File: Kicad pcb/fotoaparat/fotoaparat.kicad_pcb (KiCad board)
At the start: 2 copper layers, 120 x 85 mm, 75 parts, among them IC1 Lineární Regulátor, IC3 Lineární Regulátor Displaye, U1 STM32L496RETx, U2 MCP73833-FCI/UN, Y1 8mhz krystal

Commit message: Pokus o druhý prototyp
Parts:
- removed +BATT: Baterie, Connector_PinSocket_2.54mm:PinSocket_1x02_P2.54mm_Horizontal
- removed CAMERA: Kamera, Connector_PinSocket_2.54mm:PinSocket_2x11_P2.54mm_Vertical
- removed Free Pins: Conn_01x11_Socket, Connector_PinSocket_2.54mm:PinSocket_1x11_P2.54mm_Horizontal
- removed LCD: LCD konektor, FFC2A32-20-T:GCT_FFC2A32-20-T
- removed RX: UART, Connector_PinHeader_2.54mm:PinHeader_1x02_P2.54mm_Vertical
- removed SD CARD: GSD090012SEU, gsd09:GSD090012SEU_AMP
- removed SWD: SWD, Connector_PinHeader_2.54mm:PinHeader_1x04_P2.54mm_Vertical
- removed USB: USB Konektor, 47436:473460001
- added J1: USB Konektor, 47436:473460001, F.Cu at (207.0, 97.0)
- added J2: SWD, Connector_PinHeader_2.54mm:PinHeader_1x04_P2.54mm_Vertical, F.Cu at (155.7, 88.2)
- added J3: LCD konektor, FFC2A32-20-T:GCT_FFC2A32-20-T, F.Cu at (102.6, 97.9)
- added J4: Baterie, Connector_PinSocket_2.54mm:PinSocket_1x02_P2.54mm_Horizontal, F.Cu at (92.1, 73.8)
- added J5: GSD090012SEU, gsd09:GSD090012SEU_AMP, F.Cu at (195.0, 121.0)
- added J6: UART, Connector_PinHeader_2.54mm:PinHeader_1x02_P2.54mm_Vertical, F.Cu at (126.2, 118.5)
- added J7: Kamera, Connector_PinSocket_2.54mm:PinSocket_2x11_P2.54mm_Vertical, B.Cu at (172.2, 84.9)
- added J9: Conn_01x11_Socket, Connector_PinSocket_2.54mm:PinSocket_1x11_P2.54mm_Horizontal, F.Cu at (175.8, 71.5)
- moved H3 110.7 mm to (197.0, 63.6)
- moved H1 110.3 mm to (86.1, 140.0)
- moved R25 106.1 mm to (95.4, 73.0)
- moved R26 105.8 mm to (95.4, 77.6)
- moved S1 103.5 mm to (84.1, 94.0), turned to 90 degrees
- moved U2 100.5 mm to (94.8, 138.6), turned to 0 degrees
- moved R8 95.6 mm to (187.5, 51.1), turned to 0 degrees
- moved D1 95.3 mm to (102.4, 130.4), turned to 0 degrees
- moved D2 94.8 mm to (102.4, 133.5), turned to 0 degrees
- moved TH1 94.7 mm to (99.2, 76.4), turned to 180 degrees
- moved D3 94.5 mm to (102.4, 136.5), turned to 0 degrees
- moved R13 94.3 mm to (187.5, 65.8), turned to 0 degrees
- moved C2 90.7 mm to (114.8, 54.4), turned to 0 degrees
- moved C1 89.6 mm to (114.8, 51.4), turned to 0 degrees
- moved C5 89.0 mm to (114.8, 63.4), turned to 0 degrees
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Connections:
- net /Backlight Regulátor renamed /Backlight Regulátor en
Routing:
- net +3.3V: track 355.6 -> 17.0 mm, vias 25 -> 0
- net +3.3V LCD: track 170.2 -> 0.00 mm, vias 6 -> 0
- net GND: track 187.3 -> 18.9 mm, vias 37 -> 1
- net /d3: track 106.8 -> 25.3 mm, vias 6 -> 0
- net /d1: track 101.5 -> 24.6 mm, vias 6 -> 0
- net /d0: track 101.4 -> 27.4 mm, vias 9 -> 0
- net +BATT: track 77.7 -> 5.10 mm, vias 2 -> 0
- net /d2: track 99.5 -> 28.0 mm, vias 11 -> 0
- net /pb0: track 64.8 -> 0.00 mm, vias 5 -> 0
- net /rrst: track 49.2 -> 111.8 mm, vias 4 -> 2
- net /pb1: track 61.6 -> 0.00 mm, vias 4 -> 0
- net /pa2: track 49.7 -> 0.00 mm, vias 2 -> 0
- net /rck: track 77.0 -> 126.1 mm, vias 8 -> 0
- net Net-(IC1-EN): track 43.7 -> 0.00 mm
- net Net-(IC3-EN): track 37.0 -> 0.00 mm
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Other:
- board size 120 x 85 mm -> 129 x 86.1 mm

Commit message: Téměř dokončený 2 prototyp
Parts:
- moved R8 92.4 mm to (102.7, 87.9)
- moved R7 90.8 mm to (92.0, 66.7), turned to 90 degrees
- moved R13 86.5 mm to (108.2, 100.3)
- moved R4 79.9 mm to (103.1, 66.7), turned to 180 degrees
- moved R5 74.8 mm to (108.2, 68.4), turned to 180 degrees
- moved U2 72.0 mm to (94.9, 66.6), turned to -90 degrees
- moved D3 71.7 mm to (112.1, 65.5), turned to 90 degrees
- moved R6 70.7 mm to (112.1, 69.2), turned to -90 degrees
- moved D2 68.3 mm to (109.1, 65.5), turned to 90 degrees
- moved C6 65.9 mm to (109.7, 132.1)
- moved D1 65.0 mm to (106.1, 65.5), turned to 90 degrees
- moved C5 64.4 mm to (110.0, 127.6)
- moved C4 63.8 mm to (110.3, 124.0)
- moved C3 63.3 mm to (110.3, 120.5)
- moved R9 37.2 mm to (167.7, 85.5), turned to 180 degrees
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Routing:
- net /pa2: track 0.00 -> 184.6 mm, vias 0 -> 4
- net /pb1: track 0.00 -> 157.9 mm, vias 0 -> 4
- net /pb0: track 0.00 -> 151.9 mm, vias 0 -> 4
- net +BATT: track 5.10 -> 113.5 mm
- net Net-(IC3-EN): track 0.00 -> 67.4 mm, vias 0 -> 4
- net Net-(IC1-EN): track 0.00 -> 50.1 mm, vias 0 -> 4
- net +3.3V LCD: track 0.00 -> 41.3 mm, vias 0 -> 6
- net Net-(U2-*PG): track 0.00 -> 21.2 mm
- net Net-(U2-STAT2): track 0.00 -> 15.5 mm
- net Net-(U2-THERM): track 0.00 -> 13.5 mm
- net /Vled+: track 0.00 -> 10.5 mm
- net Net-(U2-STAT1): track 0.00 -> 8.80 mm
- net /pb12: track 51.9 -> 46.3 mm, vias 1 -> 2
- net /pd2: track 38.6 -> 42.4 mm, vias 1 -> 2
- net /im3: track 0.00 -> 3.47 mm
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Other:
- board size 129 x 86.1 mm -> 128.9 x 86.1 mm

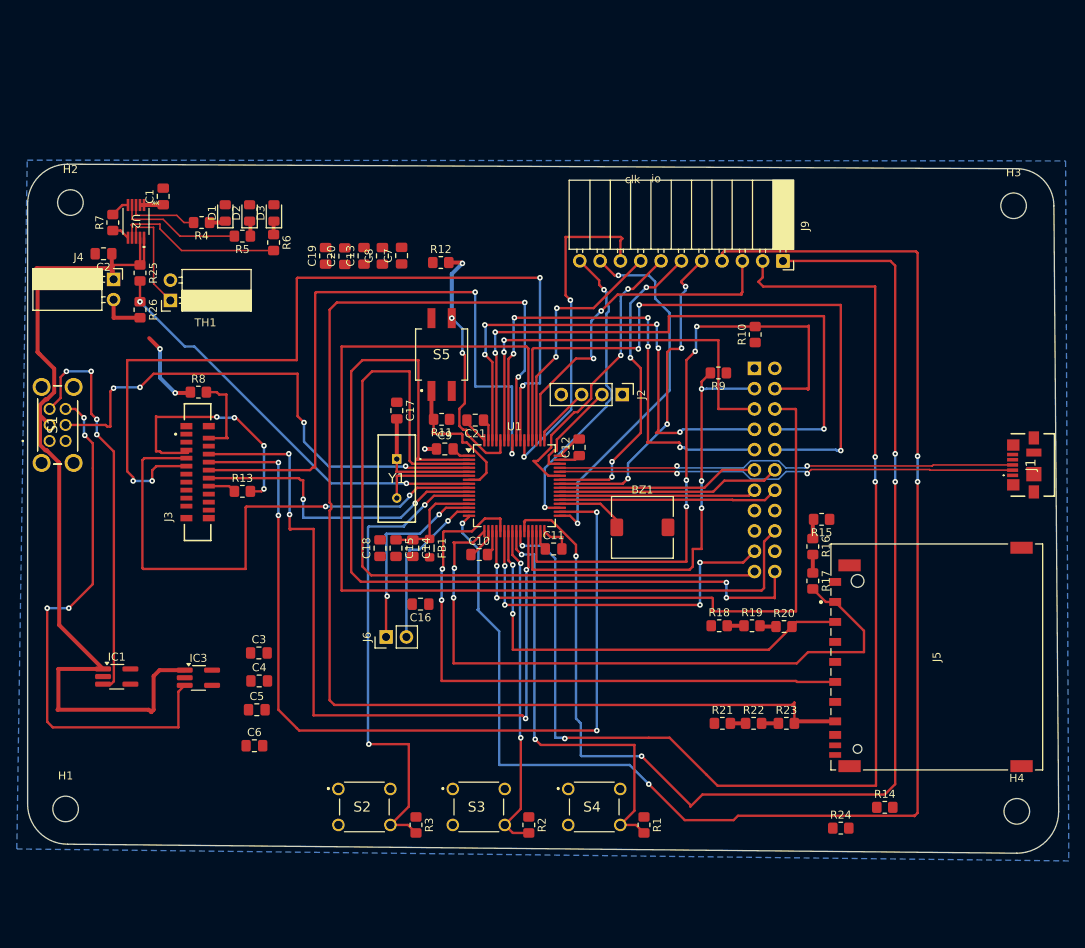
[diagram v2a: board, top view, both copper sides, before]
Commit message: Druhá deska pcb
Signálové trasy jsou víc daleko od sebe a napájecí trasy jsou více široké než v minulém designu, to by mělo zmírnit elektromagnetickou interferenci.
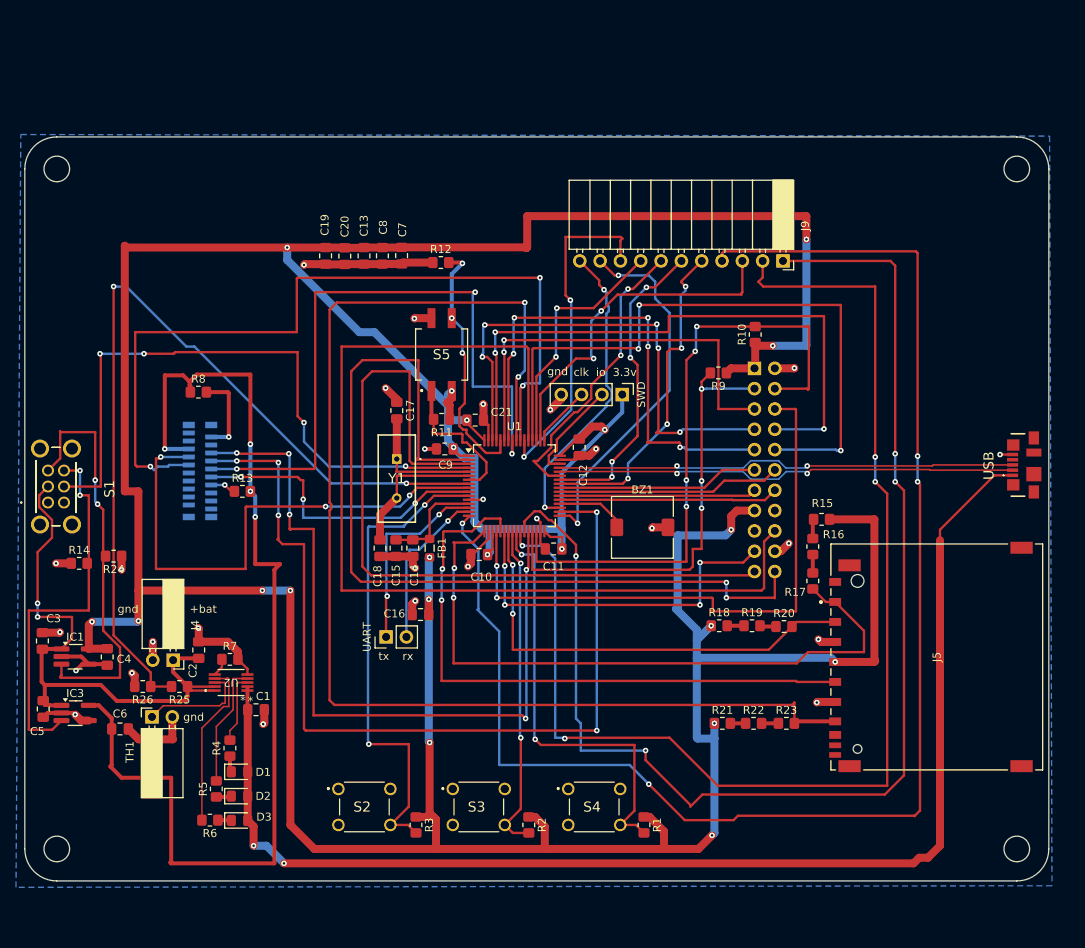
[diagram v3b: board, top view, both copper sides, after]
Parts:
- LCD: renamed from J3; moved to B.Cu
- moved R14 105.2 mm to (87.8, 109.3)
- moved R24 97.1 mm to (92.1, 108.4), turned to 180 degrees
- moved D3 76.1 mm to (107.8, 141.4), turned to 0 degrees
- moved D2 72.9 mm to (107.8, 138.4), turned to 0 degrees
- moved R6 72.6 mm to (104.1, 141.4), turned to 180 degrees
- moved D1 69.9 mm to (107.8, 135.4), turned to 0 degrees
- moved R5 69.2 mm to (104.9, 137.5), turned to 90 degrees
- moved R4 65.8 mm to (106.6, 132.4), turned to 90 degrees
- moved C1 65.2 mm to (109.9, 127.6), turned to 0 degrees
- moved U2 58.9 mm to (106.8, 124.2), turned to 180 degrees
- moved R7 56.5 mm to (106.6, 121.3), turned to 0 degrees
- moved TH1 52.1 mm to (96.9, 128.5), turned to 90 degrees
- moved R25 51.9 mm to (100.3, 124.7), turned to 180 degrees
- moved C2 50.9 mm to (102.7, 120.1), turned to 90 degrees
- moved J4 48.2 mm to (99.5, 121.4), turned to -90 degrees
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- renumbered J7 to CAMERA, J2 to SWD, J6 to UART, J1 to USB
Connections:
- IC1 pad 4: unconnected-(IC1-NC/ADJ-Pad4) -> GND
- IC3 pad 4: unconnected-(IC3-NC/ADJ-Pad4) -> GND
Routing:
- net +3.3V: track 17.0 -> 550.7 mm, vias 0 -> 21
- net VBUS: track 2.80 -> 159.1 mm, vias 0 -> 2
- net GND: track 21.3 -> 113.7 mm, vias 1 -> 28
- net +3.3V LCD: track 41.3 -> 131.3 mm, vias 6 -> 4
- net /Baterka Napětí: track 53.1 -> 109.2 mm
- net +BATT: track 113.5 -> 73.4 mm, vias 0 -> 2
- net Net-(IC3-EN): track 67.4 -> 47.6 mm, vias 4 -> 2
- net /Backlight Regulátor en: track 65.2 -> 79.6 mm
- net /osc out: track 11.8 -> 17.9 mm
- net /csx: track 107.9 -> 103.6 mm, vias 4 -> 3
- net /sda: track 68.8 -> 65.9 mm, vias 2 -> 3
- net /pb1: track 157.9 -> 160.1 mm
- net /pb0: track 151.9 -> 153.9 mm
- net Net-(IC1-EN): track 50.1 -> 51.2 mm, vias 4 -> 2
- net /scl: track 112.4 -> 113.4 mm, vias 4 -> 5
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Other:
- board size 128.9 x 86.1 mm -> 128 x 93 mm
- board text added: "+bat"
- board text added: "3.3v"
- board text added: "gnd"
- board text added: "rx"
- board text added: "tx"

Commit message: Příprava na výrobu pcb
Gerber soubory se pravděpodobně ještě změní
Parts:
- removed CAMERA: Kamera, Connector_PinSocket_2.54mm:PinSocket_2x11_P2.54mm_Vertical
- removed LCD: LCD konektor, FFC2A32-20-T:GCT_FFC2A32-20-T
- added J3: LCD konektor, FFC2A32-20-T:GCT_FFC2A32-20-T, F.Cu at (102.8, 97.7)
- added J7: Kamera, Connector_PinSocket_2.54mm:PinSocket_2x11_P2.54mm_Vertical, F.Cu at (174.7, 84.9)
- SD CARD: renamed from J5
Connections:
- U1 pad 2: /rrst -> /wrst
- U1 pad 20: /href -> /vsync
- U1 pad 3: /wrst -> /rrst
- U1 pad 37: /d0 -> /d1
- U1 pad 38: /d1 -> /d0
- U1 pad 39: /d2 -> /d3
- U1 pad 40: /d3 -> /d2
- U1 pad 52: /d4 -> /d5
- U1 pad 58: /d5 -> /d4
- U1 pad 59: /vsync -> /href
- U1 pad 61: /d6 -> /d7
- U1 pad 62: /d7 -> /d6
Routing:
- net /vsync: track 52.5 -> 77.5 mm
- net /href: track 75.6 -> 52.7 mm
- net /d5: track 62.0 -> 83.7 mm, vias 5 -> 3
- net /d4: track 82.0 -> 63.6 mm, vias 3 -> 5
- net /wr: track 46.3 -> 63.6 mm
- net GND: track 113.7 -> 129.9 mm, vias 28 -> 27
- net /d7: track 63.3 -> 77.3 mm, vias 5 -> 3
- net /rrst: track 111.8 -> 98.0 mm, vias 2 -> 0
- net /wrst: track 98.0 -> 111.7 mm, vias 0 -> 2
- net /d6: track 77.0 -> 64.0 mm, vias 3 -> 5
- net +3.3V: track 550.7 -> 538.7 mm
- net /pa2: track 184.9 -> 190.7 mm
- net /d1: track 24.6 -> 28.9 mm
- net /d3: track 25.3 -> 28.7 mm
- net /I2C_SCL: track 57.4 -> 60.8 mm
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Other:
- board text added: "Battery"

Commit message: Oprava chyb
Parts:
- removed C13, C19, C20, C8: 1u, Capacitor_SMD:C_0805_2012Metric_Pad1.18x1.45mm_HandSolder
- added C22: 1u, Capacitor_SMD:C_0805_2012Metric_Pad1.18x1.45mm_HandSolder, F.Cu at (179.1, 124.1)
- C7: value 1u -> 10u; footprint Capacitor_SMD:C_0805_2012Metric_Pad1.18x1.45mm_HandSolder -> Capacitor_THT:CP_Radial_D5.0mm_P2.50mm
- moved R8 19.6 mm to (102.8, 107.5), turned to 180 degrees
- moved R13 11.2 mm to (98.2, 95.3), turned to 180 degrees
- moved C7 6.29 mm to (128.1, 64.5), turned to -90 degrees
- turned J3 to -90 degrees
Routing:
- net /sda: track 65.9 -> 34.6 mm
- net /csx: track 103.8 -> 87.4 mm
- net GND: track 129.9 -> 118.3 mm
- net /sdo: track 38.6 -> 45.9 mm
- net +3.3V: track 538.7 -> 545.8 mm
- net /wrx d/cx: track 82.0 -> 88.4 mm, vias 2 -> 4
- net +3.3V LCD: track 131.3 -> 125.4 mm, vias 3 -> 0
- net /rst: track 97.2 -> 100.6 mm
- net /scl: track 113.5 -> 115.3 mm
- net /im3: track 3.77 -> 2.43 mm
- net /Vled+: track 10.7 -> 9.43 mm
- net Net-(IC3-EN): track 47.6 -> 46.6 mm
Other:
- board text added: "Dat0 - 7"
- board text added: "href"
- board text added: "nc"
- board text added: "rck"
- board text added: "rrst"
- board text added: "scl"
- board text added: "sda"
- board text added: "vsync"
- board text added: "wr"
- board text added: "wrst"

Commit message: Připraveno na výrobu
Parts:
- added C8: 10u, Capacitor_THT:CP_Radial_D5.0mm_P2.50mm, F.Cu at (181.5, 66.1)
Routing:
- net +3.3V: track 545.8 -> 548.7 mm
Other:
- board text added: "boot0"
- board text added: "reset"

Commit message: Úprava designu
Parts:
- removed C10, C11, C12, C14, C21, C9: 100n, Capacitor_SMD:C_0805_2012Metric_Pad1.18x1.45mm_HandSolder
- removed C15, C16, C22: 1u, Capacitor_SMD:C_0805_2012Metric_Pad1.18x1.45mm_HandSolder
- removed C17, C18: 30p, Capacitor_SMD:C_0805_2012Metric_Pad1.18x1.45mm_HandSolder
- removed C7, C8: 10u, Capacitor_THT:CP_Radial_D5.0mm_P2.50mm
- removed D1, D2, D3: LED, LED_SMD:LED_0805_2012Metric_Pad1.15x1.40mm_HandSolder
- removed FB1: 120R, Inductor_SMD:L_0805_2012Metric_Pad1.05x1.20mm_HandSolder
- removed H1, H2, H3, H4: MountingHole, MountingHole:MountingHole_3.2mm_M3
- removed IC1: Lineární Regulátor, Package_TO_SOT_SMD:TSOT-23-5_HandSoldering
- removed IC3: Lineární Regulátor Displaye, Package_TO_SOT_SMD:TSOT-23-5_HandSoldering
- removed J3: LCD konektor, FFC2A32-20-T:GCT_FFC2A32-20-T
- removed J4: Baterie, Connector_PinSocket_2.54mm:PinSocket_1x02_P2.54mm_Horizontal
- removed J7: Kamera, Connector_PinSocket_2.54mm:PinSocket_2x11_P2.54mm_Vertical
- removed J9: Conn_01x11_Socket, Connector_PinSocket_2.54mm:PinSocket_1x11_P2.54mm_Horizontal
- removed R10, R11, R12, R13, R14, R15, R16, R17, R18, R19, R20, R21, R22, R23, R24, R26, R9: 4.7k, Resistor_SMD:R_0805_2012Metric_Pad1.20x1.40mm_HandSolder
- removed R25, R7: 1k, Resistor_SMD:R_0805_2012Metric_Pad1.20x1.40mm_HandSolder
- removed R8: 2, Resistor_SMD:R_0805_2012Metric_Pad1.20x1.40mm_HandSolder
- removed S1: Zapínací spínač, mfs:MFS201N24Z
- removed S2: tlačítko doleva, mc3:MC32829
- removed S3: prostřední tlačítko, mc3:MC32829
- removed S4: tlačítko doprava, mc3:MC32829
- removed S5: spínač, cfs201mb:CFS0201MB
- removed SD CARD: GSD090012SEU, gsd09:GSD090012SEU_AMP
- removed SWD: SWD, Connector_PinHeader_2.54mm:PinHeader_1x04_P2.54mm_Vertical
- removed TH1: 10k, Connector_PinSocket_2.54mm:PinSocket_1x02_P2.54mm_Horizontal
- removed UART: UART, Connector_PinHeader_2.54mm:PinHeader_1x02_P2.54mm_Vertical
- removed USB: USB Konektor, 47436:473460001
- removed Y1: 8mhz krystal, hc4:HC49S830507030ATF
- added J1: Conn_02x01, Connector_PinHeader_2.54mm:PinHeader_2x01_P2.54mm_Vertical, F.Cu at (125.5, 64.5)
- added Q1: BC547, Package_TO_SOT_THT:TO-92_Inline, F.Cu at (151.9, 145.4)
- added Q2: BC547, Package_TO_SOT_THT:TO-92_Inline, F.Cu at (188.3, 143.6)
- added SW1: SW_Push_Dual, Tlačítko:tlačítko 6x6x12, B.Cu at (117.3, 123.4)
- added U3: Stm32 Bluepill, Stm32 Bluepill:Bluepill, F.Cu at (140.0, 81.8)
- added U4: Lcd Display, Lcd Display:ili9341, B.Cu at (195.6, 96.8)
- added U5: FJ08k, Tlačítko:FJ08K-S, B.Cu at (120.2, 147.4)
- added U6: Me6211c, Package_TO_SOT_SMD:SOT-23-5, F.Cu at (141.8, 144.5)
- added U7: VBsemi SI2312CDS-T1-GE3, Package_TO_SOT_SMD:SOT-23W_Handsoldering, F.Cu at (152.2, 132.9)
- added U8: Me6211c, Package_TO_SOT_SMD:SOT-23-5, F.Cu at (135.2, 134.4)
- added U9: Me6211c, Package_TO_SOT_SMD:SOT-23-5, F.Cu at (141.7, 123.9)
- BZ1: footprint Inductor_SMD:L_SXN_SMDRI73 -> Jiangsu:Jiangsu
- C1, C2, C3, C4, C5, C6: value 1u -> 4.7uf
- R1, R2: value 4.7k -> 100k; footprint Resistor_SMD:R_0805_2012Metric_Pad1.20x1.40mm_HandSolder -> Resistor_THT:R_Axial_DIN0207_L6.3mm_D2.5mm_P10.16mm_Horizontal
- R3: value 4.7k -> 10k; footprint Resistor_SMD:R_0805_2012Metric_Pad1.20x1.40mm_HandSolder -> Resistor_THT:R_Axial_DIN0207_L6.3mm_D2.5mm_P10.16mm_Horizontal
- R4: value 1k -> 100k; footprint Resistor_SMD:R_0805_2012Metric_Pad1.20x1.40mm_HandSolder -> Resistor_THT:R_Axial_DIN0207_L6.3mm_D2.5mm_P10.16mm_Horizontal
- R5: value 1k -> 30k; footprint Resistor_SMD:R_0805_2012Metric_Pad1.20x1.40mm_HandSolder -> Resistor_THT:R_Axial_DIN0207_L6.3mm_D2.5mm_P10.16mm_Horizontal
- R6: value 1k -> 50k; footprint Resistor_SMD:R_0805_2012Metric_Pad1.20x1.40mm_HandSolder -> Resistor_THT:R_Axial_DIN0207_L6.3mm_D2.5mm_P10.16mm_Horizontal
- U1: value STM32L496RETx -> TP4056; footprint Package_QFP:LQFP-64_10x10mm_P0.5mm -> TP4056:TP4056
- U2: value MCP73833-FCI/UN -> ov7670 fifo; footprint MCP:MSOP10_MC_MCH -> ov7670:ov7670
- moved R4 76.3 mm to (172.2, 93.4), turned to 180 degrees
- moved R5 70.2 mm to (162.6, 97.4), turned to 0 degrees
- moved C5 63.9 mm to (147.2, 124.9), turned to 90 degrees
- moved U1 61.3 mm to (200.7, 117.8), turned to 180 degrees
- moved C3 59.3 mm to (140.2, 135.4)
- moved R6 56.8 mm to (124.7, 88.5), turned to 90 degrees
- moved BZ1 50.6 mm to (178.7, 151.1)
- moved C6 45.2 mm to (137.7, 123.9), turned to 90 degrees
- moved R2 43.5 mm to (124.7, 103.0), turned to 90 degrees
- moved C2 42.9 mm to (138.2, 144.4)
- moved C4 42.5 mm to (131.6, 134.5)
- moved C1 39.6 mm to (146.2, 143.4), turned to -90 degrees
- moved R3 39.1 mm to (127.7, 103.0), turned to 90 degrees
- moved U2 18.8 mm to (102.7, 105.8), turned to 0 degrees
- moved R1 5.17 mm to (159.7, 137.0), turned to 90 degrees
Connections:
- BZ1 pad 1: /buzzer -> +BATT
- BZ1 pad 2: GND -> Net-(BZ1--)
- C1 pad 1: VBUS -> +4V
- C2 pad 1: +BATT -> +3.3V
- C3 pad 1: +BATT -> +4V
- C4 pad 1: GND -> +3.3V ov7670
- C4 pad 2: +3.3V -> GND
- C5 pad 1: +BATT -> +4V
- C6 pad 1: GND -> +3.3V lcd
- C6 pad 2: +3.3V LCD -> GND
- R1 pad 1: +3.3V -> Net-(Q1-C)
- R1 pad 2: /sw3 -> Net-(U1-OUT+)
- R2 pad 1: +3.3V -> GND
- R2 pad 2: /sw2 -> Net-(Q1-B)
- R3 pad 1: +3.3V -> GND
- R3 pad 2: /sw1 -> /tx
- R4 pad 1: Net-(D1-K) -> GND
- R4 pad 2: Net-(U2-STAT1) -> Net-(U3-pa1)
- R5 pad 1: Net-(D2-K) -> Net-(U3-pa1)
- R5 pad 2: Net-(U2-STAT2) -> +BATT
- R6 pad 1: /Indikátor Nabíjení -> Net-(Q1-B)
- R6 pad 2: Net-(U2-*PG) -> Net-(U3-pa12)
- U1 pad 1: +3.3V -> unconnected-(U1-IN+-Pad1)
- U1 pad 2: /wrst -> unconnected-(U1-IN--Pad2)
- U1 pad 3: /rrst -> Net-(U1-OUT+)
- U1 pad 4: /Backlight Regulátor en -> GND
- U1 pad 5: /osc in -> +BATT
- U1 pad 6: /osc out -> -BATT
- U2 pad 1: VBUS -> +3.3V ov7670
- U2 pad 10: +BATT -> Net-(U2-d4)
- U2 pad 2: VBUS -> GND
- U2 pad 3: Net-(U2-STAT1) -> Net-(U2-sioc)
- U2 pad 4: Net-(U2-STAT2) -> Net-(U2-siod)
- U2 pad 5: GND -> Net-(U2-vsync)
- U2 pad 6: Net-(U2-PROG) -> unconnected-(U2-href-Pad6)
- U2 pad 7: Net-(U2-*PG) -> Net-(U2-d7)
- U2 pad 9: +BATT -> Net-(U2-d5)
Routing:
- net +3.3V: track 548.7 -> 161.0 mm, vias 21 -> 0
- net GND: track 118.3 -> 410.7 mm, vias 27 -> 3
- net /pa2: track 190.7 -> 0.00 mm, vias 4 -> 0
- net Net-(U3-pa7): track 0.00 -> 169.8 mm
- net Net-(U3-pa5): track 0.00 -> 160.4 mm
- net /pb1: track 159.6 -> 0.00 mm, vias 4 -> 0
- net VBUS: track 159.1 -> 0.00 mm, vias 2 -> 0
- net /sd miso: track 157.5 -> 0.00 mm, vias 2 -> 0
- net /pb0: track 152.4 -> 0.00 mm, vias 4 -> 0
- net Net-(U3-pa6): track 0.00 -> 150.3 mm
- net Net-(Q2-B): track 0.00 -> 126.0 mm
- net /rck: track 126.0 -> 0.00 mm
- net +3.3V LCD: track 125.4 -> 0.00 mm
- net /scl: track 115.3 -> 0.00 mm, vias 4 -> 0
- net /wrst: track 111.7 -> 0.00 mm, vias 2 -> 0
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- removed copper zone on B.Cu, net GND
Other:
- board size 128 x 93 mm -> 104 x 114.5 mm
- board text removed: "+bat"
- board text removed: "3.3v"
- board text removed: "Battery"
- board text removed: "Dat0 - 7"
- board text removed: "boot0"
- board text removed: "clk"
- board text removed: "gnd"
- board text removed: "href"
- board text removed: "io"
- board text removed: "nc"
- board text removed: "rck"
- board text removed: "reset"
- board text removed: "rrst"
- board text removed: "rx"
- board text removed: "scl"
- board text removed: "sda"
- board text removed: "tx"
- board text removed: "vsync"
- board text removed: "wr"
- board text removed: "wrst"

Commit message: Úprava designu
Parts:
- added J2: Conn_01x02_Socket, Connector_PinSocket_2.54mm:PinSocket_1x02_P2.54mm_Vertical, F.Cu at (123.5, 146.0)
- added Q3: BC547, Package_TO_SOT_THT:TO-92_Inline, F.Cu at (123.2, 135.3)
- added Q4: BC547, Package_TO_SOT_THT:TO-92_Inline, F.Cu at (123.2, 141.1)
- added R10: 1k, Resistor_THT:R_Axial_DIN0207_L6.3mm_D2.5mm_P10.16mm_Horizontal, F.Cu at (109.4, 146.2)
- added R7: 1k, Resistor_THT:R_Axial_DIN0207_L6.3mm_D2.5mm_P10.16mm_Horizontal, F.Cu at (109.4, 134.1)
- added R8: 10k, Resistor_THT:R_Axial_DIN0207_L6.3mm_D2.5mm_P10.16mm_Horizontal, F.Cu at (109.4, 138.1)
- added R9: 10k, Resistor_THT:R_Axial_DIN0207_L6.3mm_D2.5mm_P10.16mm_Horizontal, F.Cu at (109.4, 142.2)
- added U10: VBsemi SI2312CDS-T1-GE3, Package_TO_SOT_SMD:SOT-23W_Handsoldering, F.Cu at (104.4, 139.2)
- added U11: VBsemi SI2312CDS-T1-GE3, Package_TO_SOT_SMD:SOT-23W_Handsoldering, F.Cu at (104.4, 143.9)
- added U12: VBsemi SI2312CDS-T1-GE3, Package_TO_SOT_SMD:SOT-23W_Handsoldering, F.Cu at (104.4, 148.7)
- U5: value FJ08k -> VBsemi SI2312CDS-T1-GE3; footprint Tlačítko:FJ08K-S -> Package_TO_SOT_SMD:SOT-23W_Handsoldering; moved to F.Cu
- moved SW1 36.3 mm to (153.1, 117.5)
- moved U5 20.4 mm to (104.4, 134.5), turned to 0 degrees
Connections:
- U3 pad 33: Net-(U3-pa3) -> Net-(U12-Gate)
- U3 pad 34: Net-(U3-pa2) -> Net-(U11-Gate)
- U5 pad 1: +3.3V -> Net-(Q3-C)
- U5 pad 2: GND -> +4V
- U5 pad 3: Net-(U3-pa2) -> Net-(J2-Pin_1)
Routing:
- net Net-(U12-Gate): track 0.00 -> 99.6 mm
- net Net-(U3-pa3): track 87.0 -> 0.00 mm
- net Net-(U3-pa2): track 85.6 -> 0.00 mm, vias 1 -> 0
- net Net-(U11-Gate): track 0.00 -> 84.8 mm
- net +4V: track 67.6 -> 125.0 mm
- net Net-(U3-pb0): track 77.8 -> 38.6 mm, vias 1 -> 0
- net Net-(Q4-C): track 0.00 -> 37.8 mm
- net Net-(J2-Pin_1): track 0.00 -> 31.7 mm, vias 0 -> 1
- net Net-(U1-OUT+): track 77.2 -> 52.1 mm
- net Net-(Q3-C): track 0.00 -> 22.5 mm
- net Net-(J2-Pin_2): track 0.00 -> 22.2 mm
- net Net-(Q2-B): track 126.0 -> 103.9 mm
- net GND: track 410.7 -> 430.9 mm, vias 3 -> 1
- net /tx: track 75.7 -> 95.5 mm
- net +3.3V: track 161.0 -> 141.3 mm, vias 0 -> 2
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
